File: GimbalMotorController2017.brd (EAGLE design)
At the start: 96.6 x 79.2 mm, 125 parts, among them J1 SL03THROUGH_HOLE, J3 APP_2POS_CONFIG5V_HORIZ, Q7 MOSFET-PCHANNEL, Q8 MOSFET-PCHANNEL, Q9 MOSFET-NCHANNELAO3404A, U1 NUP4201MR6, U2 MAX3232D, U3 CSD18533Q5A, U4 CSD18533Q5A, U5 CSD18533Q5A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

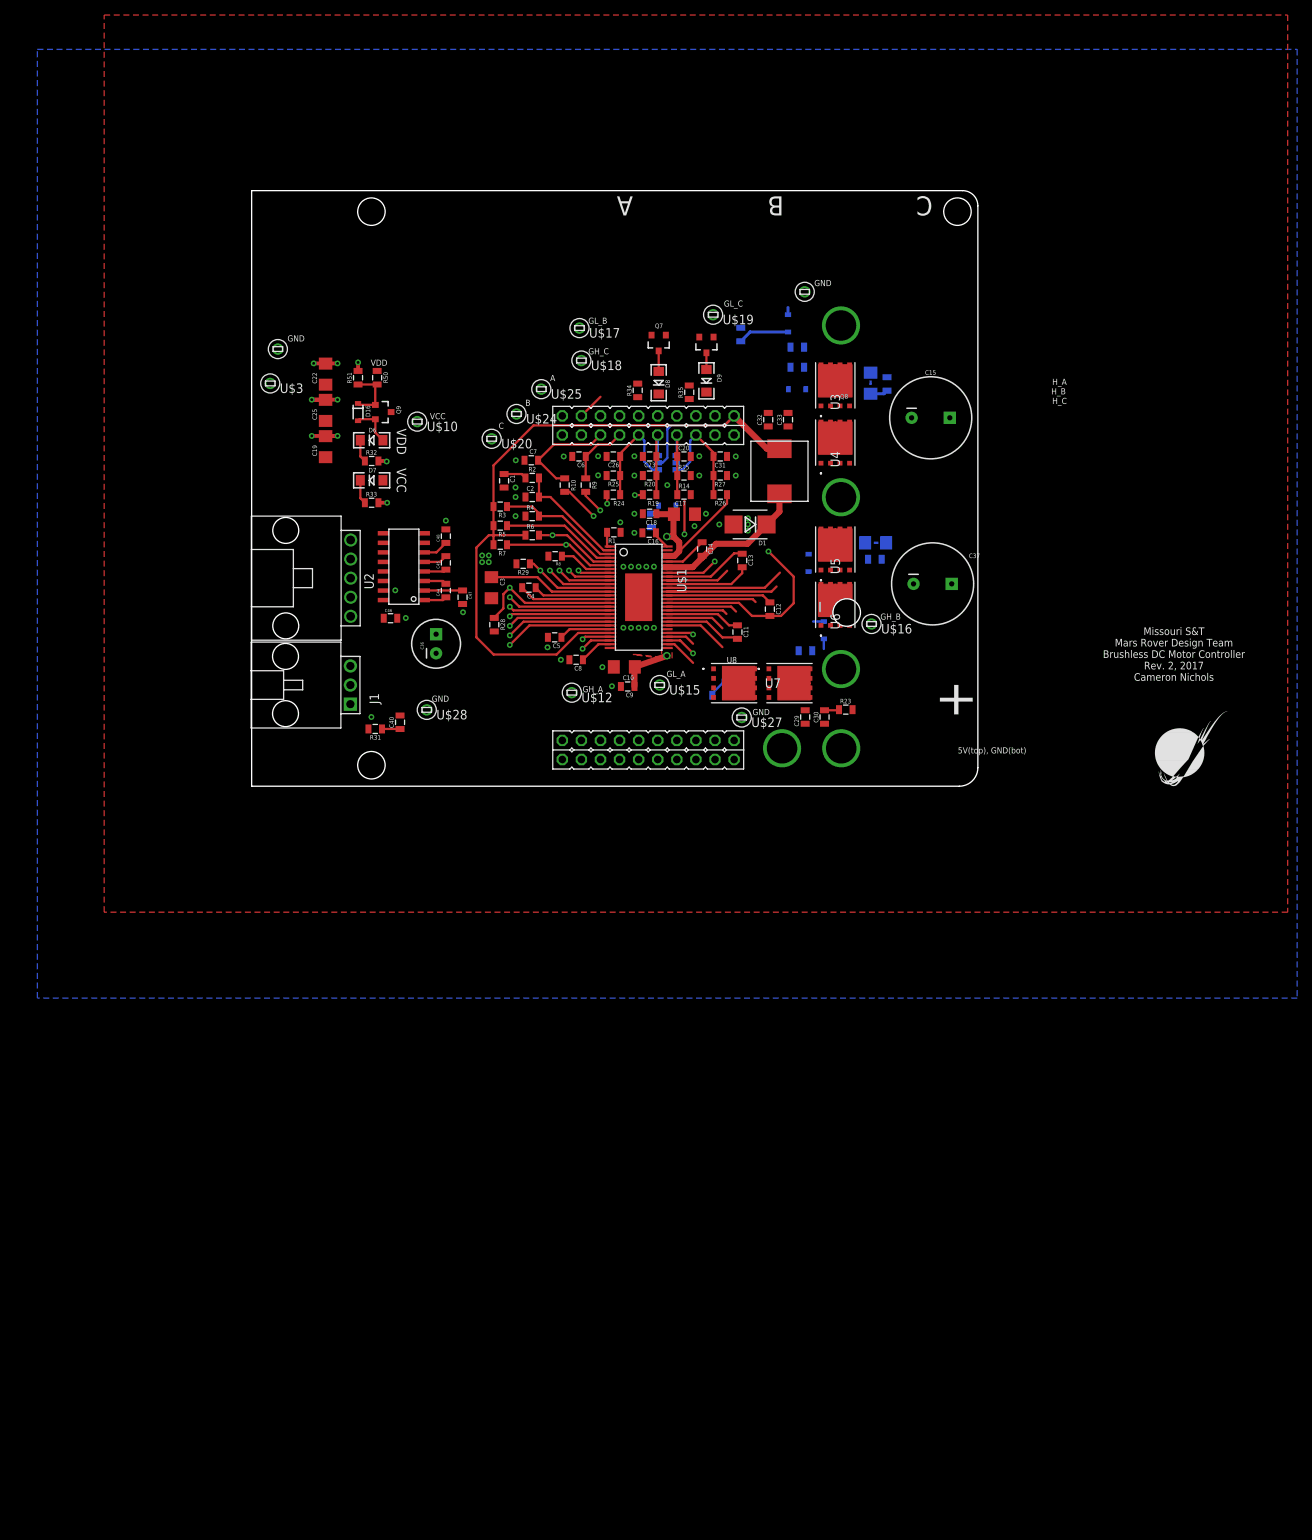
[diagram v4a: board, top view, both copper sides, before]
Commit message: Added Signatures and BOM file is now text file
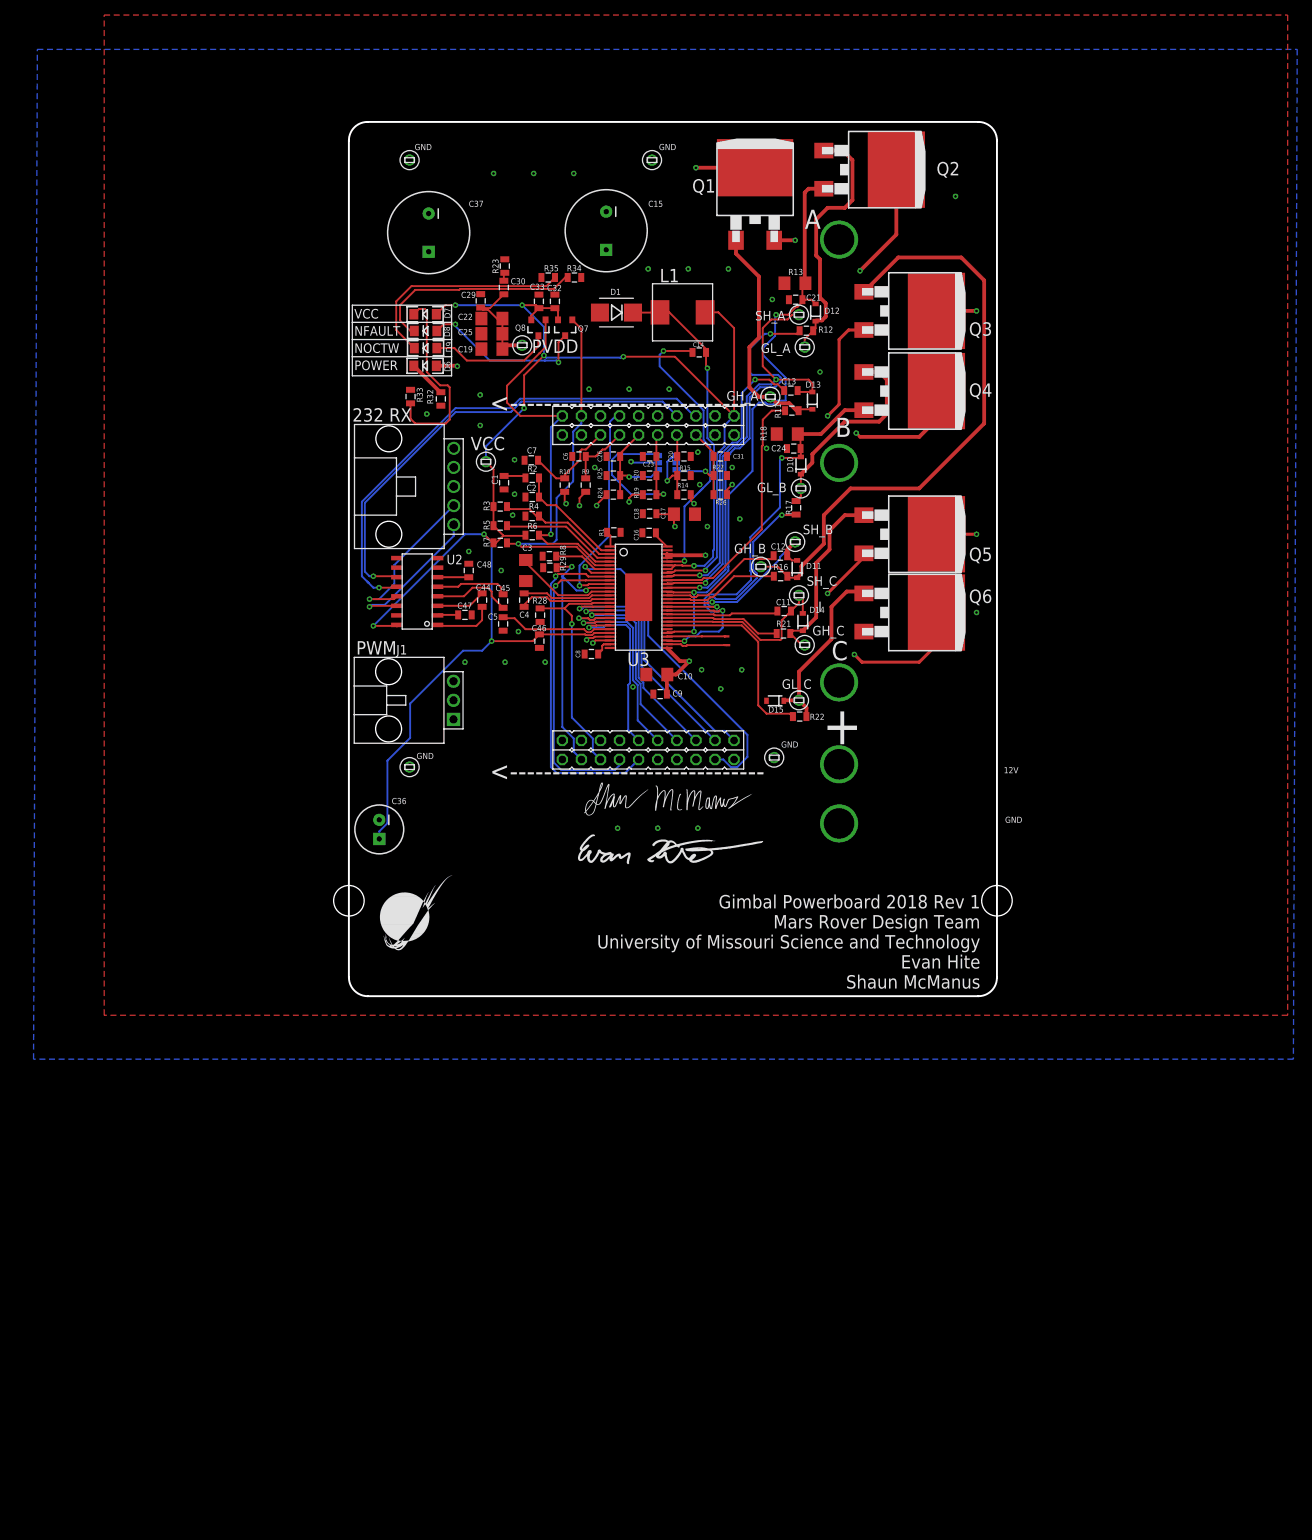
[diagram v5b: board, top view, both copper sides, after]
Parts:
- removed C40: .015u, SparkFun-Passives:0805
- removed D16: 15V, SparkFun-DiscreteSemi:SOD-323
- removed J3: APP_2POS_CONFIG5V_HORIZ, MRDT-Connectors:APP45_5V_HORIZ_CONFIG
- removed Q9: MOSFET-NCHANNELAO3404A, SparkFun-DiscreteSemi:SOT23-3
- removed R31: 100, SparkFun-Passives:0805
- removed R50: 3M, SparkFun-Passives:0805
- removed R51: 1M, SparkFun-Passives:0805
- removed U3, U4, U5, U6, U7, U8: CSD18533Q5A, CSD18533:DQJ8
- added J2: APP_2POS_CONFIG12V_HORIZ, MRDT-Connectors:APP45_12V_HORIZ_CONFIG
- added Q1, Q2, Q3, Q4, Q5, Q6: R6020ENJSMD, R6020ENJTL ROHM D2PACK:D2PACK
- added U$11: EVAN_HITE_SIGNATURE, MRDT-Signatures:EVAN_HITE_SIGNATURE
- added U$8: SHAUN_MCMANUS_SIGNATURE, MRDT-Signatures:SHAUN_MCMANUS_SIGNATURE
- R14, R19, R24, R26: value 13.2k -> 187k
- R15, R20, R25, R27: value 4.99k -> 68.1k
- R32: value 330 -> 1.2k
- moved U$9 105.4 mm to (16.4, -22.4)
- moved C37 81.7 mm to (22.9, 73.9), turned to 270 degrees
- moved U$28 79.1 mm to (52.6, 83.6)
- moved R23 74.4 mm to (33.0, 69.5), turned to 90 degrees
- moved C30 71.3 mm to (32.9, 66.6)
- moved C29 70.2 mm to (29.8, 64.8)
- moved U$26 58.3 mm to (20.3, 2.79)
- moved U$5 57.2 mm to (105.7, 77.0)
- moved U$29 55.4 mm to (20.3, 83.6)
- moved U$19 52.6 mm to (72.1, 11.7)
- moved R22 51.4 mm to (72.2, 9.53), flipped to the top, turned to 180 degrees
- moved D12 50.4 mm to (74.3, 63.3), flipped to the top, turned to 90 degrees
- moved D15 50.3 mm to (69.0, 11.6), flipped to the top, turned to 180 degrees
- moved R12 49.9 mm to (73.1, 60.9), flipped to the top
- moved C15 49.8 mm to (46.5, 74.2), turned to 270 degrees
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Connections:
- removed net N$34: R31.2, U$4.1
- removed net N$36: C15.1
- removed net N$38: D16.C, Q9.1, R50.2, R51.1
- removed net N$41: D16.A, D6.A, Q9.2
- removed net PWM_IN_NO_FILTER: J1.3, U$2.PF4
- net GND: now also J2.GND, Q6.2; no longer C40.2, J3.GND, R51.2, U4.3
- net N$13: now also Q2.1; no longer U8.4
- net N$14: now also Q3.1; no longer U6.4
- net N$15: now also Q4.1; no longer U5.4
- net N$16: now also Q1.1; no longer U7.4
- net N$17: now also Q5.1; no longer U3.4
- net N$18: now also Q6.1; no longer U4.4
- net PVDD: now also C15.1, D6.A, J2.12V, Q2.TAB, Q3.TAB, Q5.TAB; no longer J3.5V, R50.1, U3.8, U6.8, U8.8
- net PWM_IN: now also J1.3, U$2.PF4; no longer C40.1, R31.1, U$2.PA2
- net SH_A: now also Q1.TAB, Q2.2; no longer U7.8, U8.3
- net SH_B: now also Q3.2, Q4.TAB; no longer U5.8, U6.3
- net SH_C: now also Q5.2, Q6.TAB; no longer U3.3, U4.8
- net SL_A: now also Q1.2; no longer U7.3
- net SL_B: now also Q4.2; no longer U5.3
- net VCC: no longer Q9.3
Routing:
- net VCC: track 143.6 -> 244.6 mm, vias 1 -> 10
- net N$14: track 1.36 -> 79.8 mm
- net SH_A: track 26.3 -> 100.7 mm, vias 1 -> 5
- net UART_RX: track 0.00 -> 66.6 mm, vias 0 -> 1
- net UART_TX: track 0.00 -> 61.6 mm, vias 0 -> 1
- net SL_A: track 36.2 -> 83.7 mm, vias 1 -> 3
- net SL_B: track 22.2 -> 63.1 mm, vias 1 -> 3
- net GL_A: track 15.9 -> 54.2 mm, vias 0 -> 2
- net SH_C: track 48.9 -> 84.8 mm, vias 1 -> 3
- net N$30: track 5.76 -> 39.5 mm, vias 0 -> 2
- net N$16: track 2.43 -> 34.8 mm
- net N$13: track 0.00 -> 31.1 mm
- net N$27: track 0.00 -> 29.7 mm
- net PVDD: track 29.7 -> 58.6 mm, vias 2 -> 8
- net N$26: track 0.00 -> 28.5 mm
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- added copper zone on layer 2, net SH_A
- added copper zone on layer 2, net SH_B
- added copper zone on layer 2, net SH_C
- removed copper zone on layer 1, net PVDD
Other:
- board size 96.6 x 79.2 mm -> 86.2 x 116.3 mm
- board text added: "232 RX"
- board text added: "<------------------------------"
- board text added: "Gimbal Powerboard 2018 Rev 1 Mars Rover Design Team University of Missouri Science and Technology Evan Hite Shaun McManus"
- board text added: "L1"
- board text added: "NFAULT"
- board text added: "NOCTW"
- board text added: "POWER"
- board text added: "PVDD"
- board text added: "PWM"
- board text added: "Q1"
- board text added: "Q2"
- board text added: "Q3"
- board text added: "Q4"
- board text added: "Q5"
- board text added: "Q6"
- board text added: "SH_A"
- board text added: "SH_B"
- board text added: "SH_C"
- board text added: "U3"
- board text removed: "H_A"
- board text removed: "H_B"
- board text removed: "H_C"
- board text removed: "Missouri S&T Mars Rover Design Team Brushless DC Motor Controller Rev. 2, 2017 Cameron Nichols"
- board text removed: "VDD"
